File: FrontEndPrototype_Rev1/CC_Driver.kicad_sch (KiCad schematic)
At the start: 12 parts, among them U2 ADA4807-2ACP

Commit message: Checking if Branch Updates Work
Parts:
- gave numbers to parts that had none: 11

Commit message: Small Updates
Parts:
- R4: value 2k -> 1k
- RT1: value 50 -> 0
- Rf1: value 2.5k -> 1.5k
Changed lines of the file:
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@@
 			)
 		)
-		(property "Value" "2.5k"
+		(property "Value" "1.5k"
 			(at 99.06 36.4744 90)
 			(effects
@@
 			)
 		)
-		(property "Value" "2k"
+		(property "Value" "1k"
 			(at 82.55 53.34 90)
 			(effects
@@
 			)
 		)
-		(property "Value" "50"
+		(property "Value" "0"
 			(at 33.9344 57.15 90)
 			(effects

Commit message: First Pass Schematic Fixes for Power Management Board
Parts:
- R?: renamed from R4; value 1k -> 2k
- R?: renamed from RT1; value 0 -> 50
- Rf?: renamed from Rf1; value 1.5k -> 2.5k
- renumbered C1 to C?, C2 to C?, C3 to C?, Cb2 to Cb?, Cf1 to Cf?, R2 to R?, R3 to R?, R_iso1 to R_iso?

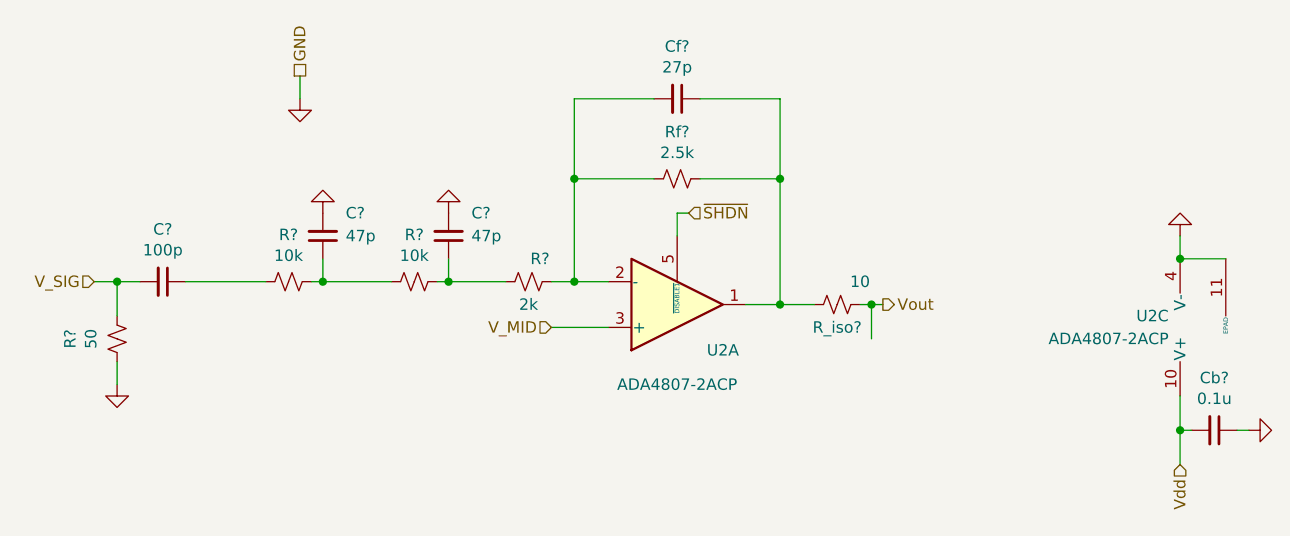
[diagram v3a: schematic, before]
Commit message: Updated Measurement Board with new 3V Reference
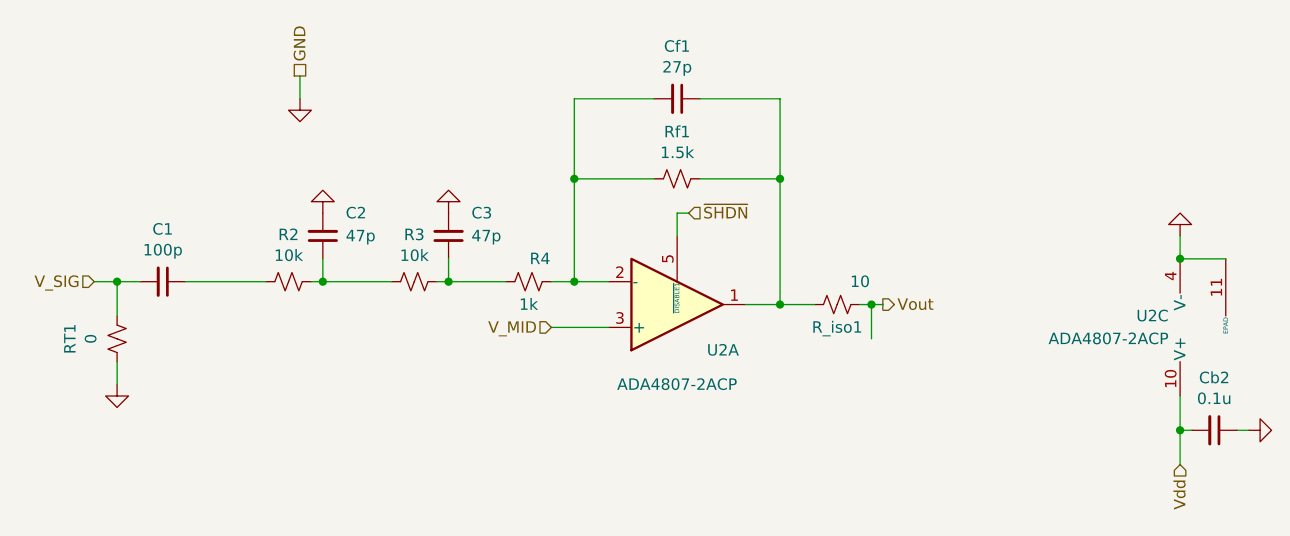
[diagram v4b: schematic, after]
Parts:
- R4: renamed from R?; value 2k -> 1k
- RT1: renamed from R?; value 50 -> 0
- Rf1: renamed from Rf?; value 2.5k -> 1.5k
- gave numbers to parts that had none: 8
